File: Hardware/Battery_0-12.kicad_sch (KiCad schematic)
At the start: 69 parts, among them J1 Conn_01x28

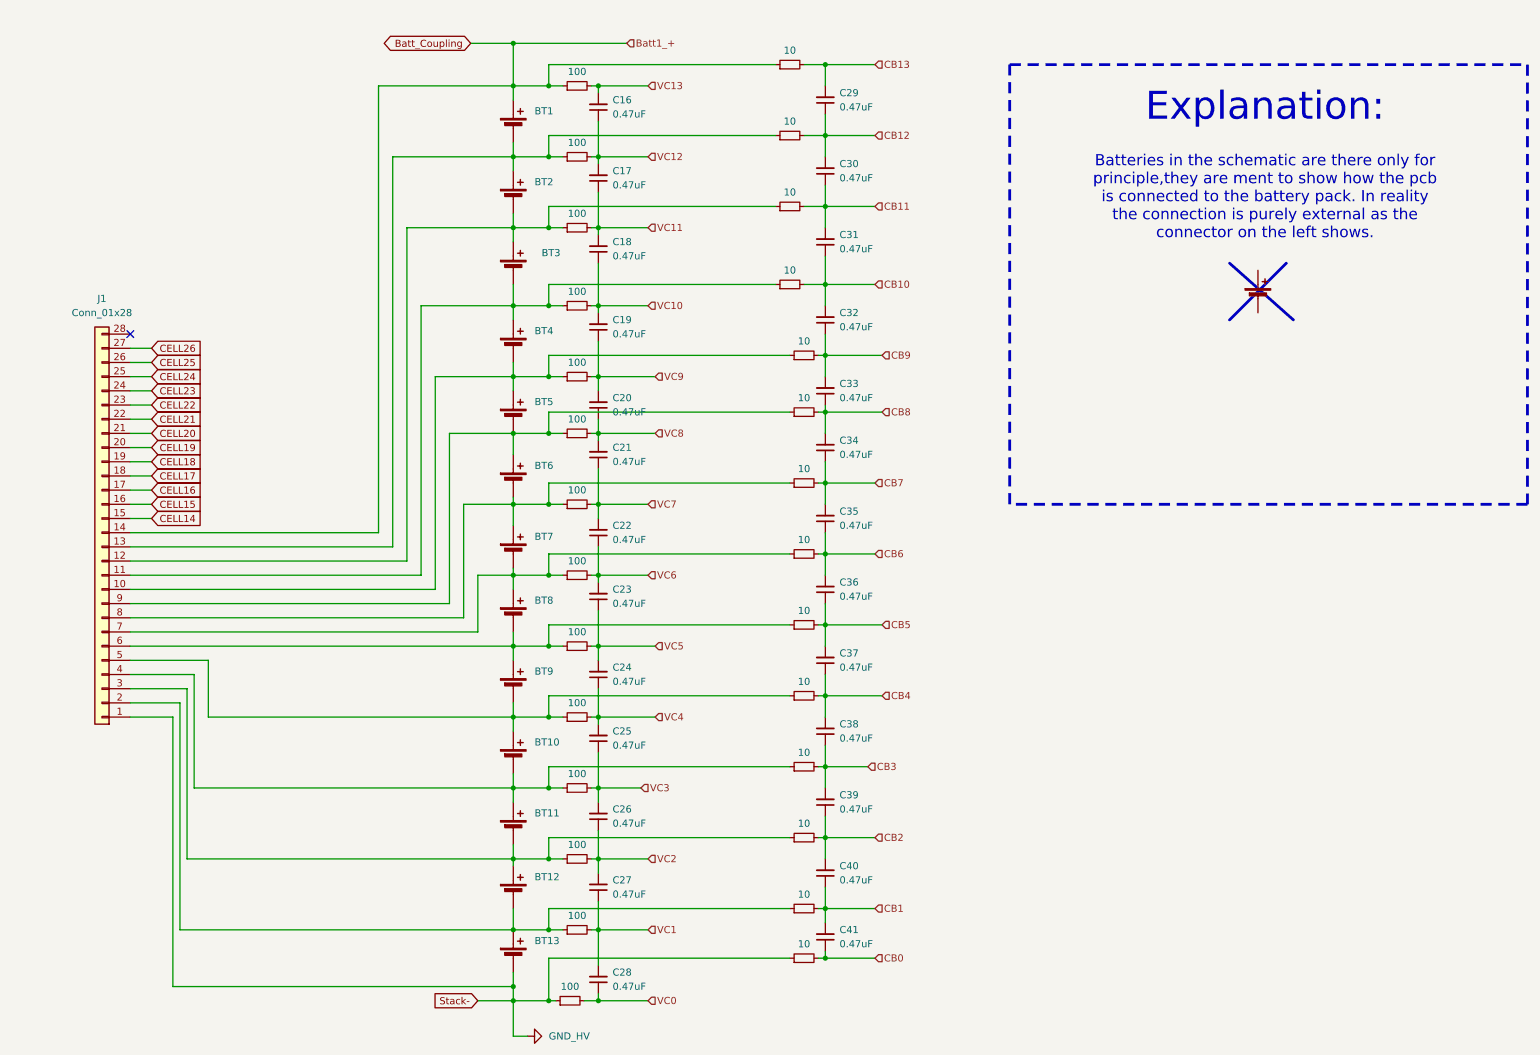
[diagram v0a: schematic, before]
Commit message: Bms plug and play, 2nd iteration with the same pinout
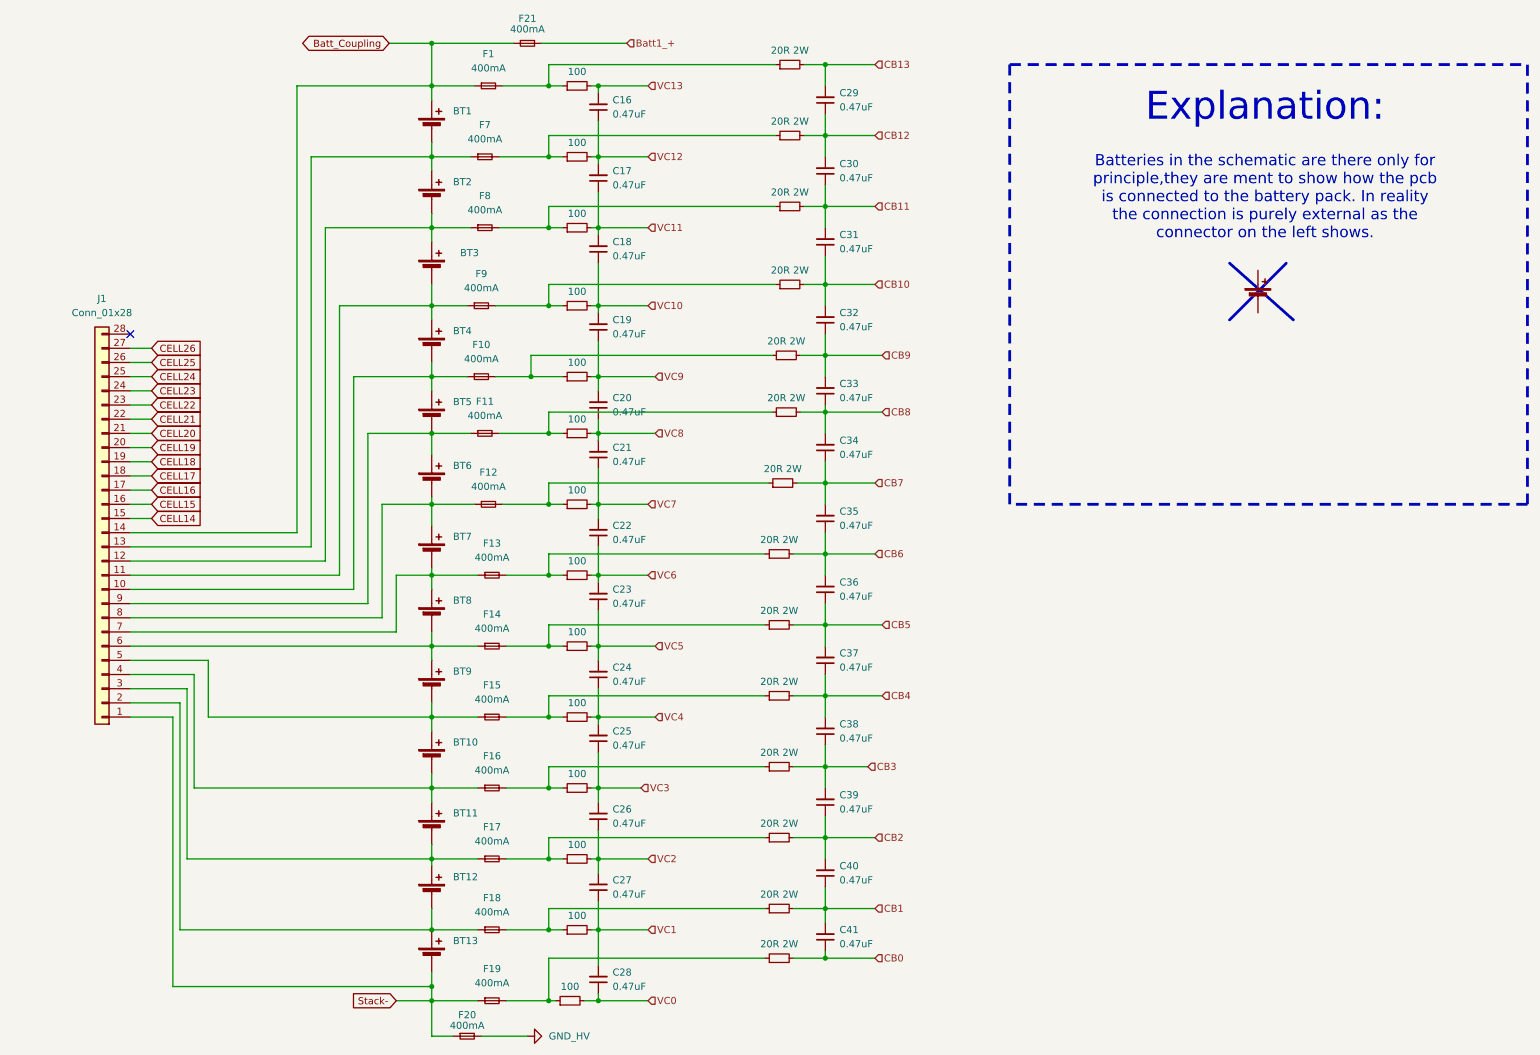
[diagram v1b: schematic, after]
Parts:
- added F1, F10, F11, F12, F13, F14, F15, F16, F17, F18, F19, F20, F21, F7, F8, F9: 400mA, Fuse:Fuse_0805_2012Metric, symbol Device:Fuse_Small
- R33, R34, R35, R36, R37, R38, R39, R40, R41, R42, R43, R44, R45, R46: value 10 -> 20R 2W; footprint footrpint:RESC6331X80N -> Resistor_SMD:R_2512_6332Metric
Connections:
- net Batt_Coupling: now also F1.1, F21.1; no longer R20.1, R33.1
- net GND_HV: now also F20.2; no longer BT13.2 (-), J1.1 (Pin_1), R19.1, R46.1
- net at BT7.2 (-), BT8.1 (+), J1.7 (Pin_7): now also F13.1; no longer R27.1, R40.1
- net at BT8.2 (-), BT9.1 (+), J1.6 (Pin_6): now also F14.1; no longer R28.1, R41.1
- net at BT6.2 (-), BT7.1 (+), J1.8 (Pin_8): now also F12.1; no longer R26.1, R39.1
- net at BT1.2 (-), BT2.1 (+), J1.13 (Pin_13): now also F7.1; no longer R21.1, R34.1
- net at BT12.2 (-), BT13.1 (+), J1.2 (Pin_2): now also F18.1; no longer R32.1, R45.1
- net at BT11.2 (-), BT12.1 (+), J1.3 (Pin_3): now also F17.1; no longer R31.1, R44.1
- net at BT10.2 (-), BT11.1 (+), J1.4 (Pin_4): now also F16.1; no longer R30.1, R43.1
- net at BT10.1 (+), BT9.2 (-), J1.5 (Pin_5): now also F15.1; no longer R29.1, R42.1
- net at BT4.2 (-), BT5.1 (+), J1.10 (Pin_10): now also F10.1; no longer R24.1, R37.1
- net at BT5.2 (-), BT6.1 (+), J1.9 (Pin_9): now also F11.1; no longer R25.1, R38.1
- net at BT2.2 (-), BT3.1 (+), J1.12 (Pin_12): now also F8.1; no longer R22.1, R35.1
- net at BT3.2 (-), BT4.1 (+), J1.11 (Pin_11): now also F9.1; no longer R23.1, R36.1
- new net: F16.2, R30.1, R43.1
- new net: F1.2, R20.1, R33.1
- new net: F19.2, R19.1, R46.1
- new net: F13.2, R27.1, R40.1
- new net: F17.2, R31.1, R44.1
- new net: F11.2, R25.1, R38.1
- new net: F14.2, R28.1, R41.1
- new net: F12.2, R26.1, R39.1
- new net: F18.2, R32.1, R45.1
- new net: F9.2, R23.1, R36.1
- new net: F7.2, R21.1, R34.1
- new net: F8.2, R22.1, R35.1
- new net: F15.2, R29.1, R42.1
- new net: F10.2, R24.1, R37.1
- new net Batt1_+: F21.2
- new net Stack-: BT13.2 (-), F19.1, F20.1, J1.1 (Pin_1)
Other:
- moved on the sheet: BT1, BT10, BT11, BT12, BT13, BT2, BT3, BT4, BT5, BT6, BT7, BT8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

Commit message: New connectors jst_xh for low voltage side of bms
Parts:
- removed J1: Conn_01x28, footrpint:HARWIN_M80-5002842, symbol Connector_Generic:Conn_01x28
- added J14: Conn_01x14, Connector_JST:JST_XH_S14B-XH-A_1x14_P2.50mm_Horizontal, symbol Connector_Generic:Conn_01x14
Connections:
- net Batt1_+ is gone; now on net Batt_Coupling: F21.2
- net Batt_Coupling: no longer BT1.1 (+), F1.1, F21.1
- net Stack-: now also J14.14 (Pin_14)
- net at BT10.2 (-), BT11.1 (+), F16.1: now also J14.11 (Pin_11)
- net at BT7.2 (-), BT8.1 (+), F13.1: now also J14.8 (Pin_8)
- net at BT8.2 (-), BT9.1 (+), F14.1: now also J14.9 (Pin_9)
- net at BT6.2 (-), BT7.1 (+), F12.1: now also J14.7 (Pin_7)
- net at BT11.2 (-), BT12.1 (+), F17.1: now also J14.12 (Pin_12)
- net at BT5.2 (-), BT6.1 (+), F11.1: now also J14.6 (Pin_6)
- net at BT10.1 (+), BT9.2 (-), F15.1: now also J14.10 (Pin_10)
- net at BT12.2 (-), BT13.1 (+), F18.1: now also J14.13 (Pin_13)
- net at BT2.2 (-), BT3.1 (+), F8.1: now also J14.3 (Pin_3)
- net at BT1.2 (-), BT2.1 (+), F7.1: now also J14.2 (Pin_2)
- net at BT3.2 (-), BT4.1 (+), F9.1: now also J14.4 (Pin_4)
- net at BT4.2 (-), BT5.1 (+), F10.1: now also J14.5 (Pin_5)
- new net: BT1.1 (+), F1.1, F21.1, J14.1 (Pin_1)
- no-connect marks 1 -> 0
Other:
- title: (none) -> Battery Management System for a high power gokart battery

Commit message: No drc errors
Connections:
- net Stack+: now reaches BT1.1 (+), F1.1, F21.1, J14.1 (Pin_1)
- net Batt_Coupling renamed Batt1_+
- net Stack-: no longer names the net of BT13.2 (-), F19.1, F20.1, J14.14 (Pin_14)
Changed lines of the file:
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@@
+	)
+	(junction
+		(at 80.645 16.51)
+		(diameter 0)
+		(color 0 0 0 0)
 	)
 	(junction
@@
 	)
 	(junction
-		(at 104.14 16.51)
-		(diameter 0)
-		(color 0 0 0 0)
-	)
-	(junction
 		(at 80.645 76.2)
 		(diameter 0)
@@
 	)
 	(junction
+		(at 93.98 194.31)
+		(diameter 0)
+		(color 0 0 0 0)
+	)
+	(junction
 		(at 101.6 187.96)
 		(diameter 0)
@@
 	(wire
 		(pts
-			(xy 100.33 16.51) (xy 104.14 16.51)
+			(xy 100.33 16.51) (xy 115.57 16.51)
 		)
 		(stroke
@@
 	(wire
 		(pts
-			(xy 73.025 13.335) (xy 73.025 16.51)
-		)
-		(stroke
-			(width 0)
-			(type default)
-		)
-	)
-	(wire
-		(pts
 			(xy 74.295 111.76) (xy 80.645 111.76)
 		)
@@
 	(wire
 		(pts
-			(xy 104.14 16.51) (xy 115.57 16.51)
+			(xy 93.98 194.31) (xy 97.79 194.31)
 		)
 		(stroke
@@
 	(wire
 		(pts
+			(xy 73.025 16.51) (xy 80.645 16.51)
+		)
+		(stroke
+			(width 0)
+			(type default)
+		)
+	)
+	(wire
+		(pts
 			(xy 80.645 49.53) (xy 80.645 52.07)
 		)
@@
 		(pts
 			(xy 80.645 137.16) (xy 40.64 137.16)
-		)
-		(stroke
-			(width 0)
-			(type default)
-		)
-	)
-	(wire
-		(pts
-			(xy 104.14 16.51) (xy 104.14 13.335)
 		)
 		(stroke
@@
 	(wire
 		(pts
+			(xy 76.835 192.405) (xy 93.98 192.405)
+		)
+		(stroke
+			(width 0)
+			(type default)
+		)
+	)
+	(wire
+		(pts
 			(xy 101.6 107.95) (xy 101.6 111.76)
 		)
@@
 	(wire
 		(pts
-			(xy 74.295 187.96) (xy 80.645 187.96)
-		)
-		(stroke
-			(width 0)
-			(type default)
-		)
-	)
-	(wire
-		(pts
 			(xy 26.67 111.76) (xy 64.135 111.76)
 		)
@@
 	(wire
 		(pts
-			(xy 104.14 13.335) (xy 73.025 13.335)
-		)
-		(stroke
-			(width 0)
-			(type default)
-		)
-	)
-	(wire
-		(pts
 			(xy 80.645 16.51) (xy 95.25 16.51)
 		)
@@
 	(wire
 		(pts
-			(xy 89.535 194.31) (xy 97.79 194.31)
+			(xy 89.535 194.31) (xy 93.98 194.31)
 		)
 		(stroke
@@
 	(wire
 		(pts
+			(xy 93.98 192.405) (xy 93.98 194.31)
+		)
+		(stroke
+			(width 0)
+			(type default)
+		)
+	)
+	(wire
+		(pts
 			(xy 104.14 111.76) (xy 101.6 111.76)
 		)
@@
 		)
 	)
-	(global_label "Stack-"
-		(shape input)
-		(at 74.295 187.96 180)
+	(global_label "Batt_Coupling"
+		(shape bidirectional)
+		(at 76.835 192.405 180)
 		(fields_autoplaced yes)
 		(effects
@@
 		)
 		(property "Intersheetrefs" "${INTERSHEET_REFS}"
-			(at 64.5365 187.96 0)
+			(at 59.6155 192.405 0)
 			(hide yes)
 			(show_name no)
@@
 		)
 	)
-	(global_label "Batt_Coupling"
-		(shape bidirectional)
+	(global_label "Stack+"
+		(shape input)
 		(at 73.025 16.51 180)
 		(fields_autoplaced yes)
@@
 		)
 		(property "Intersheetrefs" "${INTERSHEET_REFS}"
-			(at 55.8055 16.51 0)
+			(at 63.2665 16.51 0)
 			(hide yes)
 			(show_name no)
